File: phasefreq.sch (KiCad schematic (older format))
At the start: 95 parts, among them J1 Power Input, J2 RF Input, J3 LO Input, J4 VCO Tune, U1 LM317_3PinPackage, U2 LM337_SOT223, U3 ADCMP564, U4 AD9901, U5 LM4040DIZ-2.5, U6 AD8676, U7 AD8676

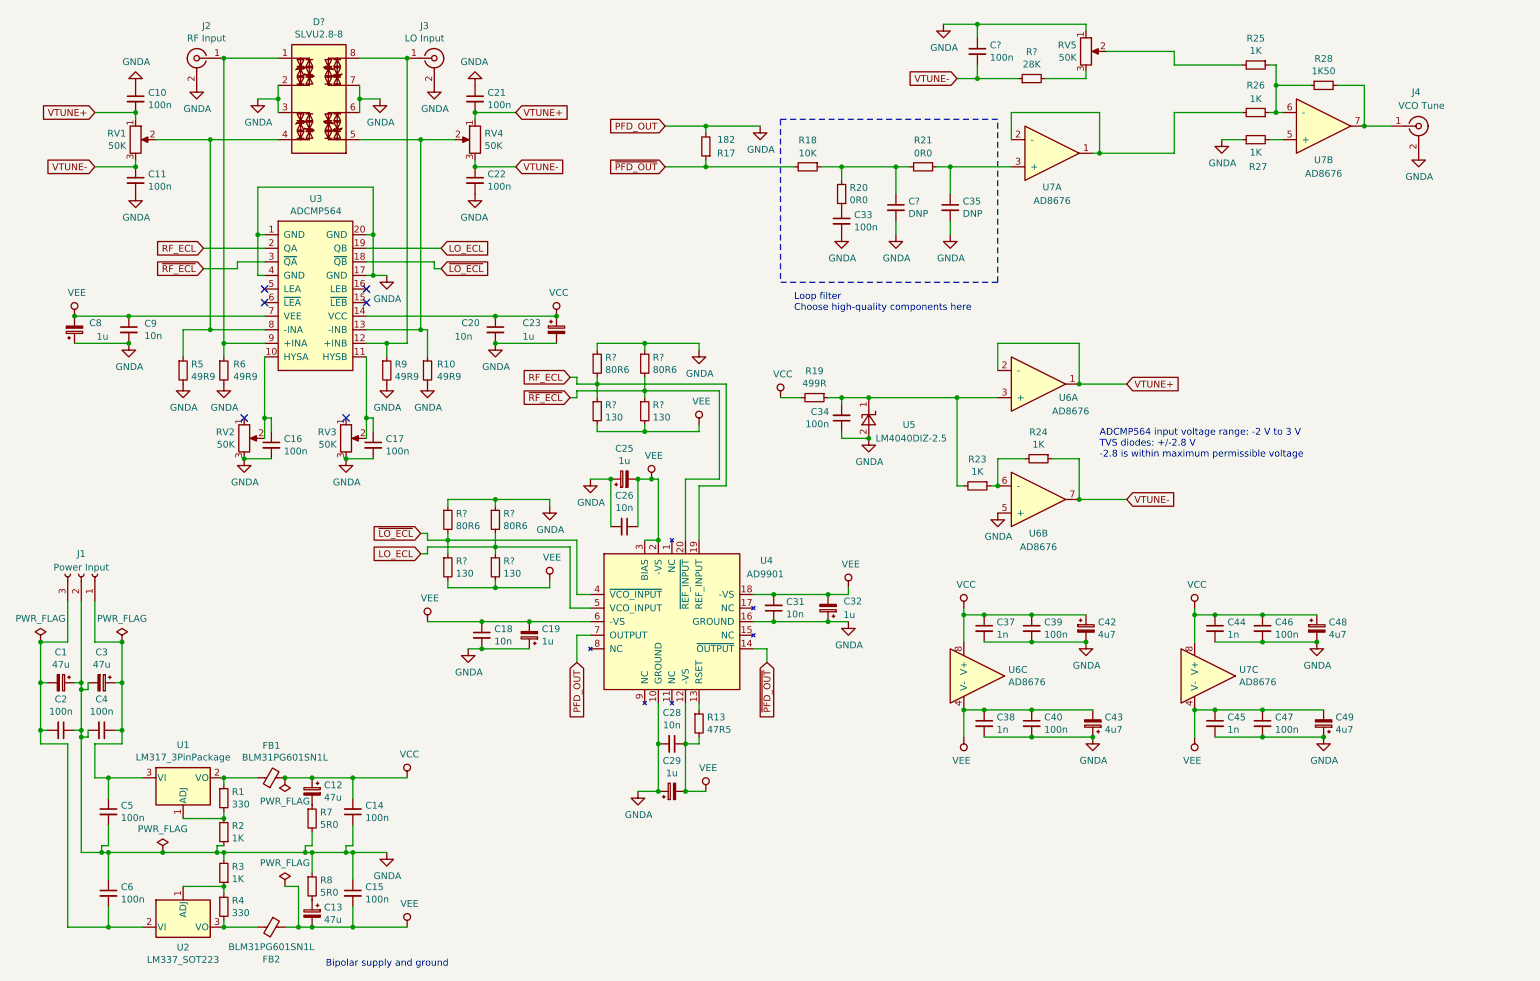
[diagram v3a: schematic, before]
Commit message: Finished schematic, relabeled components, ready for layout
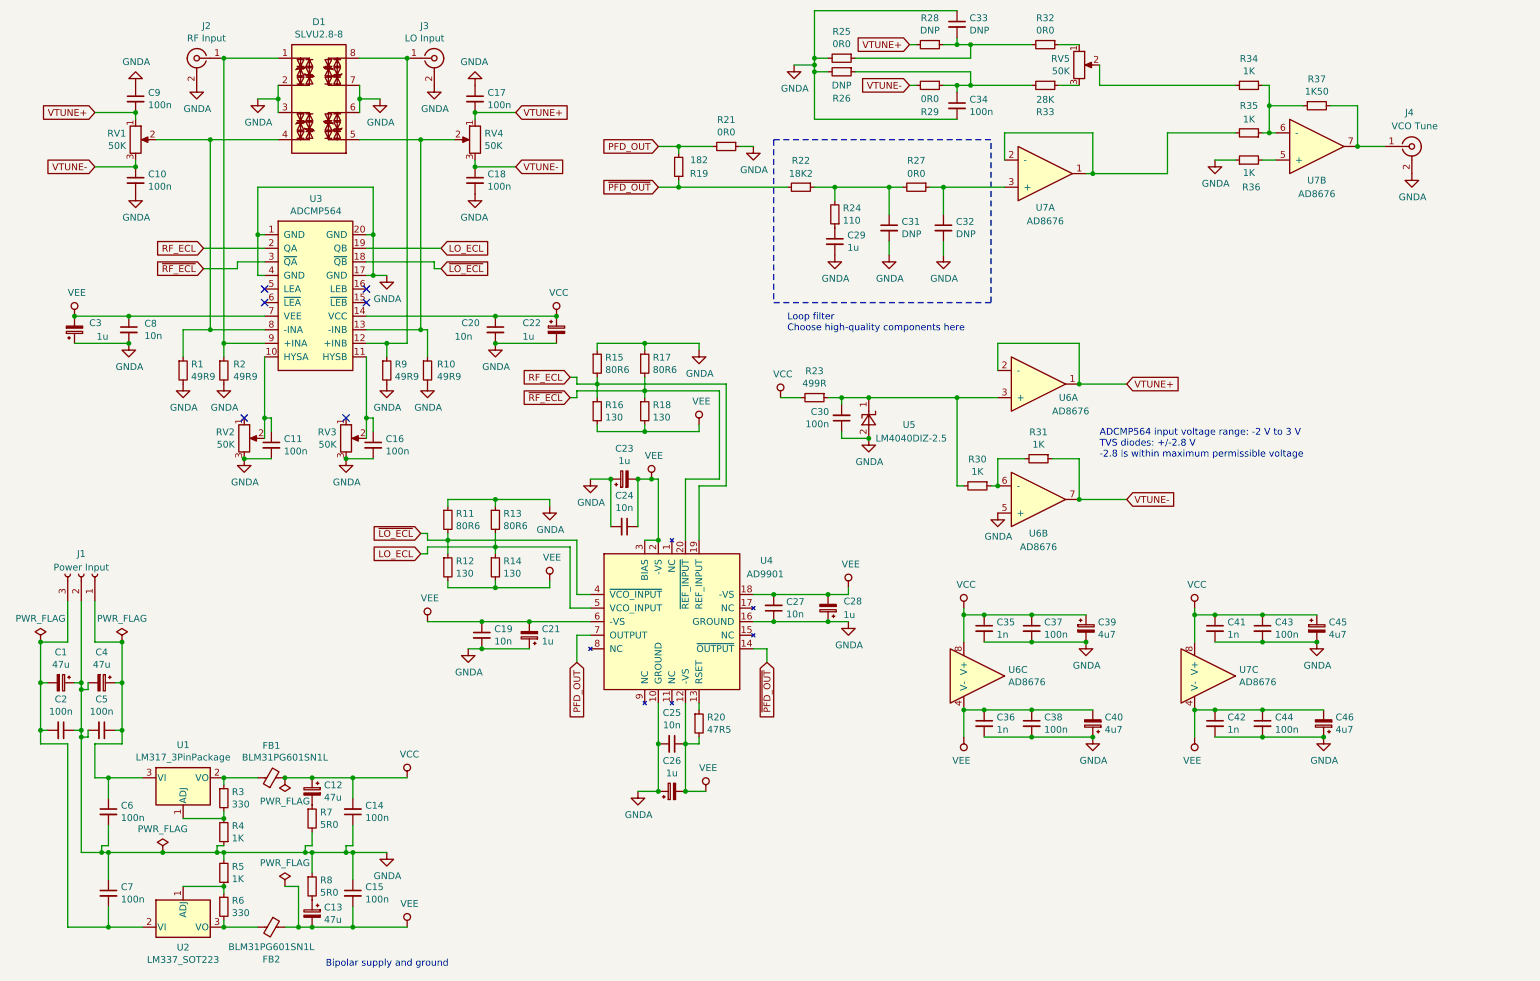
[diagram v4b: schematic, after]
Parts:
- added C33: DNP, Capacitor_SMD:C_0603_1608Metric, symbol Device:C_Small
- added R21, R25, R29, R32: 0R0, Resistor_SMD:R_0603_1608Metric, symbol Device:R_Small
- added R26, R28: DNP, Resistor_SMD:R_0603_1608Metric, symbol Device:R_Small
- C29: renamed from C33; value 100n -> 1u
- C34: renamed from C?; footprint (none) -> Capacitor_SMD:C_0603_1608Metric
- R11, R12, R13, R14, R15, R16, R17, R18, R33: renamed from R?; footprint (none) -> Resistor_SMD:R_0603_1608Metric
- R22: renamed from R18; value 10K -> 18K2
- R24: renamed from R20; value 0R0 -> 110
- gave numbers to parts that had none: 2
- renumbered C11 to C10, C16 to C11, C17 to C16, C21 to C17, C22 to C18, C18 to C19, C19 to C21, C23 to C22, C25 to C23, C26 to C24, C28 to C25, C29 to C26, C31 to C27, C32 to C28, C8 to C3, C34 to C30, C35 to C32, C37 to C35, C38 to C36, C39 to C37, C40 to C38, C42 to C39, C3 to C4, C43 to C40, C44 to C41, C45 to C42, C46 to C43, C47 to C44, C48 to C45, C49 to C46, C4 to C5, C5 to C6, C6 to C7, C9 to C8, C10 to C9, R5 to R1, R17 to R19, R6 to R2, R13 to R20, R19 to R23, R21 to R27, R1 to R3, R23 to R30, R24 to R31, R25 to R34, R26 to R35, R27 to R36, R28 to R37, R2 to R4, R3 to R5, R4 to R6
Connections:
- net GNDA: now also C34.2, C33.1, R21.1, R25.2, R26.2; no longer C34.1, R19.2, RV5.1, U4.7 (OUTPUT)
- net VTUNE+: now also R28.2
- net VTUNE-: now also R29.2; no longer C34.2, R33.1
- net at RV5.3: now also R33.1; no longer R33.2
- new net: R32.1, RV5.1
- new net: C33.2, R25.1, R28.1, R32.2
- new net: C34.1, R26.1, R29.1, R33.2
- new net PFD_OUT: R19.2, R21.2, U4.7 (OUTPUT)
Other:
- moved on the sheet: C29, C31, C32, C34, J4, R19, R22, R24, R27, R33, R34, R35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

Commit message: fixed some cap footprints, started layout
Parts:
- C12, C13: footprint Capacitor_Tantalum_SMD:CP_EIA-7343-43_Kemet-X -> Capacitor_Tantalum_SMD:CP_EIA-3216-18_Kemet-A
- C21, C28: footprint Capacitor_SMD:C_0603_1608Metric -> Capacitor_Tantalum_SMD:CP_EIA-1608-10_AVX-L
- C22, C23, C26, C3, C39, C40, C45, C46: footprint Capacitor_Tantalum_SMD:CP_EIA-3528-21_Kemet-B -> Capacitor_Tantalum_SMD:CP_EIA-1608-10_AVX-L
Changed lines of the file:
@@
 F 0 "C22" H 4300 3000 50  0000 L CNN
 F 1 "1u" H 4300 2900 50  0000 L CNN
-F 2 "Capacitor_Tantalum_SMD:CP_EIA-3528-21_Kemet-B" H 4588 2800 50  0001 C CNN
+F 2 "Capacitor_Tantalum_SMD:CP_EIA-1608-10_AVX-L" H 4588 2800 50  0001 C CNN
 F 3 "~" H 4550 2950 50  0001 C CNN
 	1    4550 2950
@@
 F 0 "C26" V 5625 6350 50  0000 C CNN
 F 1 "1u" V 5534 6350 50  0000 C CNN
-F 2 "Capacitor_Tantalum_SMD:CP_EIA-3528-21_Kemet-B" H 5400 6350 50  0001 C CNN
+F 2 "Capacitor_Tantalum_SMD:CP_EIA-1608-10_AVX-L" H 5400 6350 50  0001 C CNN
 F 3 "~" H 5400 6350 50  0001 C CNN
 	1    5400 6350
@@
 F 0 "C21" H 4258 5154 50  0000 R CNN
 F 1 "1u" H 4258 5245 50  0000 R CNN
-F 2 "Capacitor_SMD:C_0603_1608Metric" H 4350 5200 50  0001 C CNN
+F 2 "Capacitor_Tantalum_SMD:CP_EIA-1608-10_AVX-L" H 4350 5200 50  0001 C CNN
 F 3 "~" H 4350 5200 50  0001 C CNN
 	1    4350 5200
@@
 F 0 "C45" H 10238 5196 50  0000 L CNN
 F 1 "4u7" H 10238 5105 50  0000 L CNN
-F 2 "Capacitor_Tantalum_SMD:CP_EIA-3528-21_Kemet-B" H 10150 5150 50  0001 C CNN
+F 2 "Capacitor_Tantalum_SMD:CP_EIA-1608-10_AVX-L" H 10150 5150 50  0001 C CNN
 F 3 "~" H 10150 5150 50  0001 C CNN
 	1    10150 5150
@@
 F 0 "C46" H 10112 5804 50  0000 R CNN
 F 1 "4u7" H 10112 5895 50  0000 R CNN
-F 2 "Capacitor_Tantalum_SMD:CP_EIA-3528-21_Kemet-B" H 10200 5850 50  0001 C CNN
+F 2 "Capacitor_Tantalum_SMD:CP_EIA-1608-10_AVX-L" H 10200 5850 50  0001 C CNN
 F 3 "~" H 10200 5850 50  0001 C CNN
 	1    10200 5850
@@
 F 0 "C13" H 2662 7296 50  0000 R CNN
 F 1 "47u" H 2662 7205 50  0000 R CNN
-F 2 "Capacitor_Tantalum_SMD:CP_EIA-7343-43_Kemet-X" H 2750 7250 50  0001 C CNN
+F 2 "Capacitor_Tantalum_SMD:CP_EIA-3216-18_Kemet-A" H 2750 7250 50  0001 C CNN
 F 3 "~" H 2750 7250 50  0001 C CNN
 	1    2750 7250
@@
 F 0 "C12" H 2662 6396 50  0000 R CNN
 F 1 "47u" H 2662 6305 50  0000 R CNN
-F 2 "Capacitor_Tantalum_SMD:CP_EIA-7343-43_Kemet-X" H 2750 6350 50  0001 C CNN
+F 2 "Capacitor_Tantalum_SMD:CP_EIA-3216-18_Kemet-A" H 2750 6350 50  0001 C CNN
 F 3 "~" H 2750 6350 50  0001 C CNN
 	1    2750 6350
@@
 F 0 "C23" V 5275 4050 50  0000 C CNN
 F 1 "1u" V 5184 4050 50  0000 C CNN
-F 2 "Capacitor_Tantalum_SMD:CP_EIA-3528-21_Kemet-B" H 5050 4050 50  0001 C CNN
+F 2 "Capacitor_Tantalum_SMD:CP_EIA-1608-10_AVX-L" H 5050 4050 50  0001 C CNN
 F 3 "~" H 5050 4050 50  0001 C CNN
 	1    5050 4050
@@
 F 0 "C39" H 8538 5196 50  0000 L CNN
 F 1 "4u7" H 8538 5105 50  0000 L CNN
-F 2 "Capacitor_Tantalum_SMD:CP_EIA-3528-21_Kemet-B" H 8450 5150 50  0001 C CNN
+F 2 "Capacitor_Tantalum_SMD:CP_EIA-1608-10_AVX-L" H 8450 5150 50  0001 C CNN
 F 3 "~" H 8450 5150 50  0001 C CNN
 	1    8450 5150
@@
 F 0 "C40" H 8412 5804 50  0000 R CNN
 F 1 "4u7" H 8412 5895 50  0000 R CNN
-F 2 "Capacitor_Tantalum_SMD:CP_EIA-3528-21_Kemet-B" H 8500 5850 50  0001 C CNN
+F 2 "Capacitor_Tantalum_SMD:CP_EIA-1608-10_AVX-L" H 8500 5850 50  0001 C CNN
 F 3 "~" H 8500 5850 50  0001 C CNN
 	1    8500 5850
@@
 F 0 "C3" H 1200 2900 50  0000 R CNN
 F 1 "1u" H 1250 3000 50  0000 R CNN
-F 2 "Capacitor_Tantalum_SMD:CP_EIA-3528-21_Kemet-B" H 1038 2800 50  0001 C CNN
+F 2 "Capacitor_Tantalum_SMD:CP_EIA-1608-10_AVX-L" H 1038 2800 50  0001 C CNN
 F 3 "~" H 1000 2950 50  0001 C CNN
 	1    1000 2950
@@
 F 0 "C28" H 6300 4950 50  0000 L CNN
 F 1 "1u" H 6350 5050 50  0000 L CNN
-F 2 "Capacitor_SMD:C_0603_1608Metric" H 6550 5000 50  0001 C CNN
+F 2 "Capacitor_Tantalum_SMD:CP_EIA-1608-10_AVX-L" H 6550 5000 50  0001 C CNN
 F 3 "~" H 6550 5000 50  0001 C CNN
 	1    6550 5000

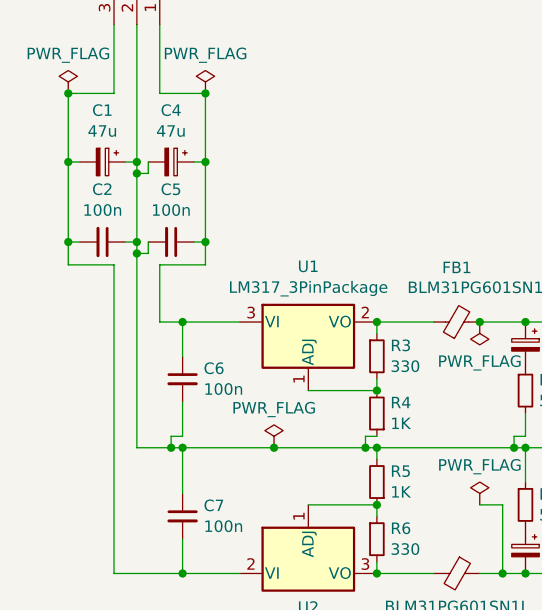
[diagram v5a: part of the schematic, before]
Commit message: basic layout of board, removed superfluous caps
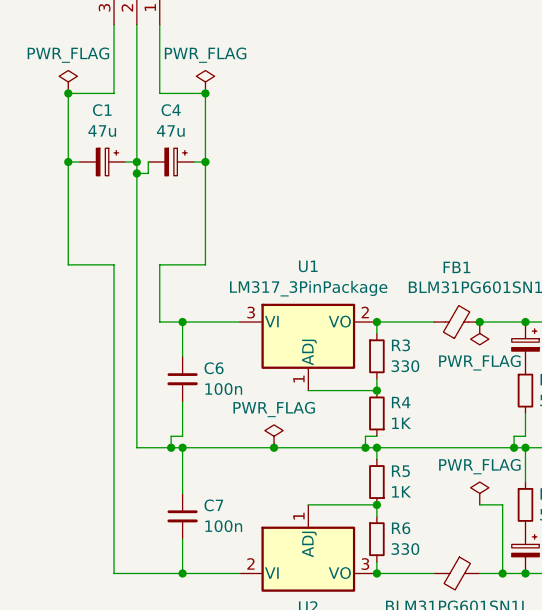
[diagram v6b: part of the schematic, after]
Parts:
- removed C2, C5: 100n, Capacitor_SMD:C_0603_1608Metric, symbol Device:C_Small
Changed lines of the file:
@@
 Wire Wire Line
 	950  4950 950  5250
-Wire Wire Line
-	1100 5950 1050 5950
-Wire Wire Line
-	1100 5900 1100 5950
-Wire Wire Line
-	1050 5600 1050 5900
 Connection ~ 1050 5600
 Wire Wire Line
@@
 Wire Wire Line
 	1050 4950 1050 5550
-Wire Wire Line
-	1050 5900 1050 5950
-Connection ~ 1050 5900
-Wire Wire Line
-	1000 5900 1050 5900
 Wire Wire Line
 	1050 5550 1050 5600
@@
 Wire Wire Line
 	750  5550 750  5250
-Connection ~ 750  5900
 Wire Wire Line
 	750  5550 800  5550
 Wire Wire Line
-	750  5900 750  5550
-Wire Wire Line
-	750  5900 800  5900
-Wire Wire Line
-	750  6000 750  5900
-Wire Wire Line
 	950  6000 750  6000
-Connection ~ 1350 5900
 Wire Wire Line
 	1350 6000 1150 6000
-Wire Wire Line
-	1350 5900 1350 6000
 Connection ~ 1350 5550
 Wire Wire Line
-	1350 5900 1300 5900
-Wire Wire Line
-	1350 5550 1350 5900
-Wire Wire Line
 	1350 5550 1300 5550
 Wire Wire Line
@@
 Wire Wire Line
 	1150 5250 1350 5250
-$Comp
-L Device:C_Small C5
-U 1 1 5D1EB9D3
-P 1200 5900
-F 0 "C5" V 971 5900 50  0000 C CNN
-F 1 "100n" V 1062 5900 50  0000 C CNN
-F 2 "Capacitor_SMD:C_0603_1608Metric" H 1200 5900 50  0001 C CNN
-F 3 "~" H 1200 5900 50  0001 C CNN
-	1    1200 5900
-	0    1    1    0
-$EndComp
-$Comp
-L Device:C_Small C2
-U 1 1 5D1EB343
-P 900 5900
-F 0 "C2" V 671 5900 50  0000 C CNN
-F 1 "100n" V 762 5900 50  0000 C CNN
-F 2 "Capacitor_SMD:C_0603_1608Metric" H 900 5900 50  0001 C CNN
-F 3 "~" H 900 5900 50  0001 C CNN
-	1    900  5900
-	0    1    1    0
-$EndComp
 $Comp
 L Device:CP_Small C1
@@
 	1150 6250 1250 6250
 Wire Wire Line
-	1050 5950 1050 6800
-Connection ~ 1050 5950
-Wire Wire Line
 	950  7350 950  6000
 $Comp
@@
 Wire Wire Line
 	8550 1000 8550 1150
+Wire Wire Line
+	1350 5550 1350 6000
+Wire Wire Line
+	750  5550 750  6000
+Wire Wire Line
+	1050 5600 1050 6800
 $EndSCHEMATC

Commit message: added mounting holes and test points to sch, added ferrite beads to op amp supplies
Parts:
- added FB3, FB4, FB5, FB6: BLM18PG221SZ1D, Inductor_SMD:L_0603_1608Metric, symbol Device:Ferrite_Bead_Small
- added H1, H2, H3, H4: M4, MountingHole:MountingHole_4.3mm_M4_Pad_Via, symbol Mechanical:MountingHole_Pad
- added TP1: VCC, TestPoint:TestPoint_THTPad_D1.5mm_Drill0.7mm, symbol Connector:TestPoint
- added TP2: GND, TestPoint:TestPoint_THTPad_D1.5mm_Drill0.7mm, symbol Connector:TestPoint
- added TP3: VEE, TestPoint:TestPoint_THTPad_D1.5mm_Drill0.7mm, symbol Connector:TestPoint
- added TP4: VT+, TestPoint:TestPoint_THTPad_D1.5mm_Drill0.7mm, symbol Connector:TestPoint
- added TP5: VT-, TestPoint:TestPoint_THTPad_D1.5mm_Drill0.7mm, symbol Connector:TestPoint
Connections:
- net GNDA: now also H1.1, H2.1, H3.1, H4.1, TP2.1
- net VCC: now also FB3.1, FB5.1, TP1.1; no longer C35.1, C37.1, C39.1, C41.1, C43.1, C45.1, U6.8 (V+), U7.8 (V+)
- net VEE: now also FB4.2, FB6.2, TP3.1; no longer C36.1, C38.1, C40.2, C42.1, C44.1, C46.2, U6.4 (V-), U7.4 (V-)
- net VTUNE+: now also TP4.1
- net VTUNE-: now also TP5.1
- new net: C41.1, C43.1, C45.1, FB5.2, U7.8 (V+)
- new net: C42.1, C44.1, C46.2, FB6.1, U7.4 (V-)
- new net: C36.1, C38.1, C40.2, FB4.1, U6.4 (V-)
- new net: C35.1, C37.1, C39.1, FB3.2, U6.8 (V+)
